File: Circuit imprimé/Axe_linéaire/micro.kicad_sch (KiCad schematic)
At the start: 2 parts

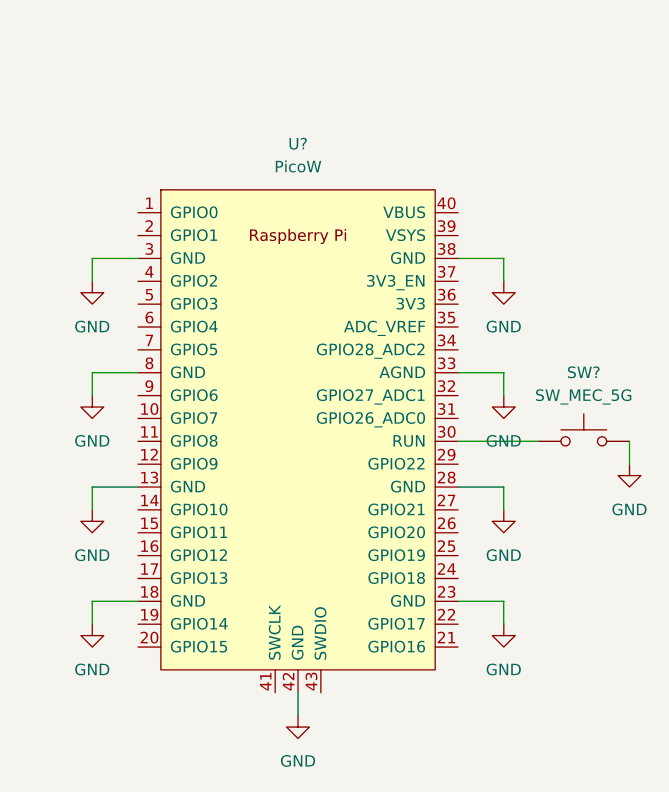
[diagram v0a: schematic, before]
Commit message: Ajout du transitor d'OR de l'alim
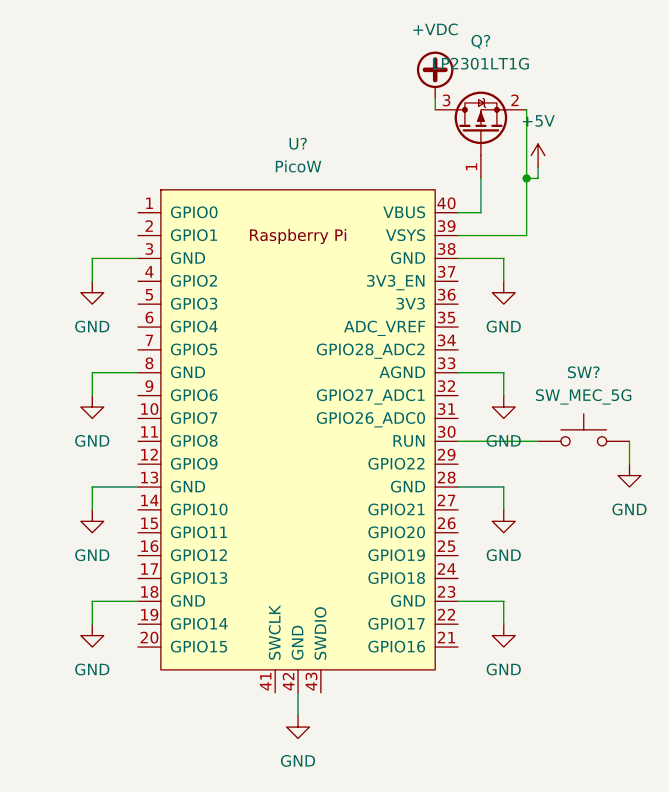
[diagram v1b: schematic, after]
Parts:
- added Q?: LP2301LT1G, Package_TO_SOT_SMD:SOT-23, symbol Transistor_FET:VP0610T
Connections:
- net +5V: now reaches U?.39 (VSYS)
- net +5V: now also Q?.2 (S)
- net at U?.40 (VBUS): now also Q?.1 (G)
- new net +VDC: Q?.3 (D)

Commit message: choix et création des Connector_FFC
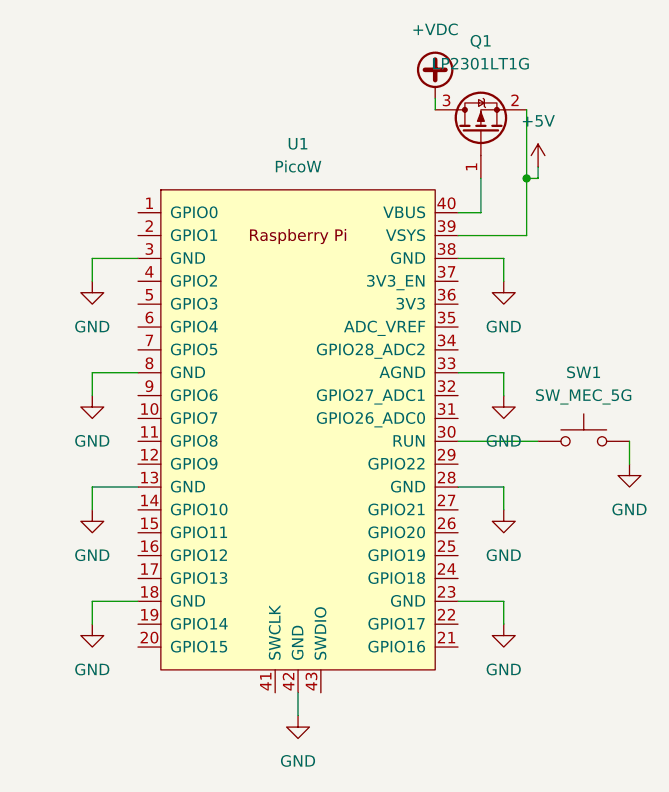
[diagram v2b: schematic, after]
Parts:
- gave numbers to parts that had none: 3
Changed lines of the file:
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@@
   (symbol (lib_id "power:+5V") (at 167.64 39.37 0) (unit 1)
     (in_bom yes) (on_board yes) (fields_autoplaced)
-    (property "Reference" "#PWR?" (id 0) (at 167.64 43.18 0)
+    (property "Reference" "#PWR011" (id 0) (at 167.64 43.18 0)
       (effects (font (size 1.27 1.27)) hide)
     )
@@
   (symbol (lib_id "power:GND") (at 163.83 64.77 0) (unit 1)
     (in_bom yes) (on_board yes) (fields_autoplaced)
-    (property "Reference" "#PWR?" (id 0) (at 163.83 71.12 0)
+    (property "Reference" "#PWR08" (id 0) (at 163.83 71.12 0)
       (effects (font (size 1.27 1.27)) hide)
     )
@@
   (symbol (lib_id "power:GND") (at 163.83 90.17 0) (unit 1)
     (in_bom yes) (on_board yes) (fields_autoplaced)
-    (property "Reference" "#PWR?" (id 0) (at 163.83 96.52 0)
+    (property "Reference" "#PWR010" (id 0) (at 163.83 96.52 0)
       (effects (font (size 1.27 1.27)) hide)
     )
@@
   (symbol (lib_id "Transistor_FET:VP0610T") (at 161.29 35.56 90) (unit 1)
     (in_bom yes) (on_board yes) (fields_autoplaced)
-    (property "Reference" "Q?" (id 0) (at 161.29 25.4 90))
+    (property "Reference" "Q1" (id 0) (at 161.29 25.4 90))
     (property "Value" "LP2301LT1G" (id 1) (at 161.29 27.94 90))
     (property "Footprint" "Package_TO_SOT_SMD:SOT-23" (id 2) (at 163.195 30.48 0)
@@
   (symbol (lib_id "power:GND") (at 163.83 77.47 0) (unit 1)
     (in_bom yes) (on_board yes) (fields_autoplaced)
-    (property "Reference" "#PWR?" (id 0) (at 163.83 83.82 0)
+    (property "Reference" "#PWR09" (id 0) (at 163.83 83.82 0)
       (effects (font (size 1.27 1.27)) hide)
     )
@@
   (symbol (lib_id "power:GND") (at 118.11 90.17 0) (unit 1)
     (in_bom yes) (on_board yes) (fields_autoplaced)
-    (property "Reference" "#PWR?" (id 0) (at 118.11 96.52 0)
+    (property "Reference" "#PWR04" (id 0) (at 118.11 96.52 0)
       (effects (font (size 1.27 1.27)) hide)
     )
@@
   (symbol (lib_id "power:+VDC") (at 156.21 31.75 0) (unit 1)
     (in_bom yes) (on_board yes) (fields_autoplaced)
-    (property "Reference" "#PWR?" (id 0) (at 156.21 34.29 0)
+    (property "Reference" "#PWR06" (id 0) (at 156.21 34.29 0)
       (effects (font (size 1.27 1.27)) hide)
     )
@@
   (symbol (lib_id "RPi_Pico:PicoW") (at 140.97 68.58 0) (unit 1)
     (in_bom yes) (on_board yes) (fields_autoplaced)
-    (property "Reference" "U?" (id 0) (at 140.97 36.83 0))
+    (property "Reference" "U1" (id 0) (at 140.97 36.83 0))
     (property "Value" "PicoW" (id 1) (at 140.97 39.37 0))
     (property "Footprint" "RPi_PicoW:RPi_Pico_SMD_TH" (id 2) (at 140.97 68.58 90)
@@
   (symbol (lib_id "power:GND") (at 140.97 100.33 0) (unit 1)
     (in_bom yes) (on_board yes) (fields_autoplaced)
-    (property "Reference" "#PWR?" (id 0) (at 140.97 106.68 0)
+    (property "Reference" "#PWR05" (id 0) (at 140.97 106.68 0)
       (effects (font (size 1.27 1.27)) hide)
     )
@@
   (symbol (lib_id "power:GND") (at 118.11 77.47 0) (unit 1)
     (in_bom yes) (on_board yes) (fields_autoplaced)
-    (property "Reference" "#PWR?" (id 0) (at 118.11 83.82 0)
+    (property "Reference" "#PWR03" (id 0) (at 118.11 83.82 0)
       (effects (font (size 1.27 1.27)) hide)
     )
@@
   (symbol (lib_id "power:GND") (at 118.11 64.77 0) (unit 1)
     (in_bom yes) (on_board yes) (fields_autoplaced)
-    (property "Reference" "#PWR?" (id 0) (at 118.11 71.12 0)
+    (property "Reference" "#PWR02" (id 0) (at 118.11 71.12 0)
       (effects (font (size 1.27 1.27)) hide)
     )
@@
   (symbol (lib_id "power:GND") (at 118.11 52.07 0) (unit 1)
     (in_bom yes) (on_board yes) (fields_autoplaced)
-    (property "Reference" "#PWR?" (id 0) (at 118.11 58.42 0)
+    (property "Reference" "#PWR01" (id 0) (at 118.11 58.42 0)
       (effects (font (size 1.27 1.27)) hide)
     )
@@
   (symbol (lib_id "Switch:SW_MEC_5G") (at 172.72 69.85 0) (unit 1)
     (in_bom yes) (on_board yes) (fields_autoplaced)
-    (property "Reference" "SW?" (id 0) (at 172.72 62.23 0))
+    (property "Reference" "SW1" (id 0) (at 172.72 62.23 0))
     (property "Value" "SW_MEC_5G" (id 1) (at 172.72 64.77 0))
     (property "Footprint" "Library:Tactile Button" (id 2) (at 172.72 64.77 0)
@@
   (symbol (lib_id "power:GND") (at 163.83 52.07 0) (unit 1)
     (in_bom yes) (on_board yes) (fields_autoplaced)
-    (property "Reference" "#PWR?" (id 0) (at 163.83 58.42 0)
+    (property "Reference" "#PWR07" (id 0) (at 163.83 58.42 0)
       (effects (font (size 1.27 1.27)) hide)
     )
@@
   (symbol (lib_id "power:GND") (at 177.8 72.39 0) (unit 1)
     (in_bom yes) (on_board yes) (fields_autoplaced)
-    (property "Reference" "#PWR?" (id 0) (at 177.8 78.74 0)
-      (effects (font (size 1.27 1.27)) hide)
-    )
+    (property "Reference" "#PWR012" (id 0) (at 177.8 78.74 0)
+      (effects (font (size 1.27 1.27)) hide)
+    )

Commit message: Ajout des protections sur l'alimentation
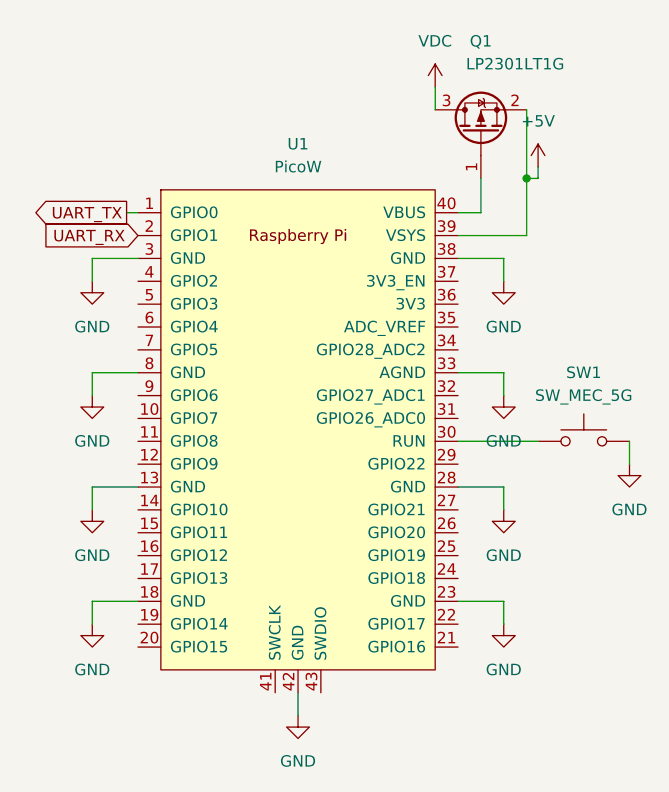
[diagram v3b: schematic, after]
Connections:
- net UART_TX: now reaches U1.1 (GPIO0)
- net UART_RX: now reaches U1.2 (GPIO1)
- net +VDC renamed VDC
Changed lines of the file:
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@@
+    (stroke (width 0) (type default) (color 0 0 0 0))
+  )
+  (wire (pts (xy 121.92 44.45) (xy 123.19 44.45))
     (stroke (width 0) (type default) (color 0 0 0 0))
   )
@@
     (stroke (width 0) (type default) (color 0 0 0 0))
   )
-  (wire (pts (xy 156.21 31.75) (xy 156.21 33.02))
+  (wire (pts (xy 156.21 30.48) (xy 156.21 33.02))
     (stroke (width 0) (type default) (color 0 0 0 0))
   )
@@
     )
   )
+  (global_label "UART_TX" (shape output) (at 121.92 44.45 180) (fields_autoplaced)
+    (effects (font (size 1.27 1.27)) (justify right))
+    (property "Intersheet References" "${INTERSHEET_REFS}" (id 0) (at 111.7055 44.3706 0)
+      (effects (font (size 1.27 1.27)) (justify right) hide)
+    )
+  )
+  (global_label "UART_RX" (shape input) (at 123.19 46.99 180) (fields_autoplaced)
+    (effects (font (size 1.27 1.27)) (justify right))
+    (property "Intersheet References" "${INTERSHEET_REFS}" (id 0) (at 112.6731 46.9106 0)
+      (effects (font (size 1.27 1.27)) (justify right) hide)
+    )
+  )
   (symbol (lib_id "power:+5V") (at 167.64 39.37 0) (unit 1)
     (in_bom yes) (on_board yes) (fields_autoplaced)
@@
     (pin "1")
   )
+  (symbol (lib_id "power:VDC") (at 156.21 30.48 0) (unit 1)
+    (in_bom yes) (on_board yes) (fields_autoplaced)
+    (property "Reference" "#PWR?" (id 0) (at 156.21 33.02 0)
+      (effects (font (size 1.27 1.27)) hide)
+    )
+    (property "Value" "VDC" (id 1) (at 156.21 25.4 0))
+    (property "Footprint" "" (id 2) (at 156.21 30.48 0)
+      (effects (font (size 1.27 1.27)) hide)
+    )
+    (property "Datasheet" "" (id 3) (at 156.21 30.48 0)
+      (effects (font (size 1.27 1.27)) hide)
+    )
+    (pin "1")
+  )
   (symbol (lib_id "power:GND") (at 163.83 90.17 0) (unit 1)
     (in_bom yes) (on_board yes) (fields_autoplaced)
@@
   )
   (symbol (lib_id "Transistor_FET:VP0610T") (at 161.29 35.56 90) (unit 1)
-    (in_bom yes) (on_board yes) (fields_autoplaced)
+    (in_bom yes) (on_board yes)
     (property "Reference" "Q1" (id 0) (at 161.29 25.4 90))
-    (property "Value" "LP2301LT1G" (id 1) (at 161.29 27.94 90))
+    (property "Value" "LP2301LT1G" (id 1) (at 165.1 27.94 90))
     (property "Footprint" "Package_TO_SOT_SMD:SOT-23" (id 2) (at 163.195 30.48 0)
       (effects (font (size 1.27 1.27) italic) (justify left) hide)
@@
       (effects (font (size 1.27 1.27)) hide)
     )
-    (pin "1")
-  )
-  (symbol (lib_id "power:+VDC") (at 156.21 31.75 0) (unit 1)
-    (in_bom yes) (on_board yes) (fields_autoplaced)
-    (property "Reference" "#PWR06" (id 0) (at 156.21 34.29 0)
-      (effects (font (size 1.27 1.27)) hide)
-    )
-    (property "Value" "+VDC" (id 1) (at 156.21 24.13 0))
-    (property "Footprint" "" (id 2) (at 156.21 31.75 0)
-      (effects (font (size 1.27 1.27)) hide)
-    )
-    (property "Datasheet" "" (id 3) (at 156.21 31.75 0)
-      (effects (font (size 1.27 1.27)) hide)
-    )
